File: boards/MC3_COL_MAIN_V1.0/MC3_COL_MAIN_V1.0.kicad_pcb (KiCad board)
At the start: 4 copper layers, 66 x 66 mm, 109 parts, among them J1 SUPPLY_IN, J10 MOTOR, J11 MOTOR, J12 CAN, J2 SWD, J3 ENC_leaf1, J4 ENC_leaf2, J5 ENC_leaf3, J6 ENC_leaf4, J7 MOTOR, J8 MOTOR, J9 MOTOR, Q1 AO4407C, SW1 SKRKAEE020, U1 AMS1117-3.3, U2 STM32F412RET6, U3 DRV8214RTER, U4 DRV8214RTER, U5 DRV8214RTER, U6 DRV8214RTER, U7 DRV8214RTER, U8 TJA1051T/3, Y1 8MHz

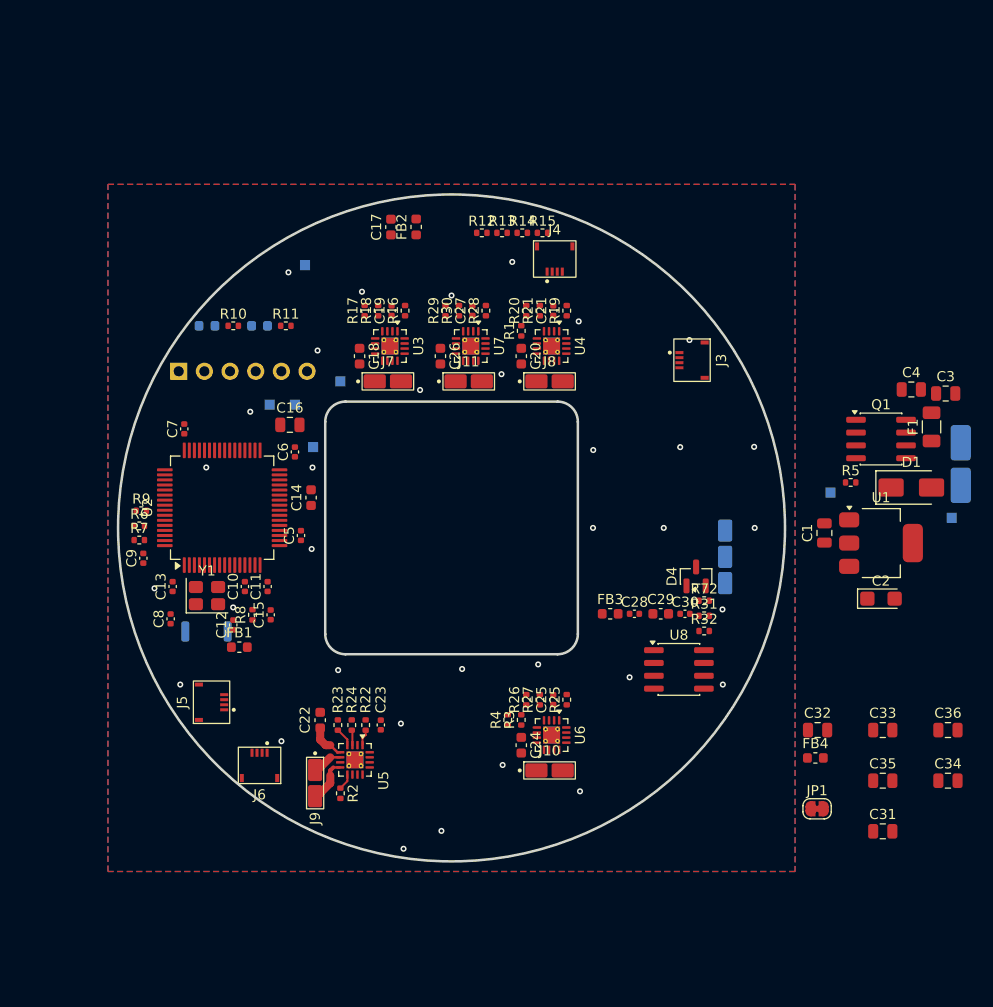
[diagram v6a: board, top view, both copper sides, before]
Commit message: PCB: power block placed on the east rim, input chain routed
Deleted the 19 GND stitching vias I had scattered across the board - they were
obstructing placement and one of them, at (75.726, 94.017), was sitting in the
middle of the MCU's 0.5 mm pin row and shorting RC_OUT_leaf3 to GND. My
collision check when generating them had a gap. They go back last, once the
layout settles. The 4 GND vias the user placed by hand are untouched.

Power block moved from its parking spot east of the outline into the free wedge
between the encoder FFC at 41 deg and the CAN block at 354 deg, which is where
the vault wants the supply pads - next to the CAN pads as one machine loom.
Layout was verified against pad overlap, rim and aperture before any part moved:
J1 (125, 89) on B.Cu, F1 (119.5, 88), Q1 (117, 92.5), D1 (124, 92) flipped so
its VIN_PROT pad faces the chain, R5 (113.9, 96.5), bulk C1/C3/C4 at y 96.5,
FB4 (116.5, 99), C32 (120, 99.5), U1 (118, 104), C2 (124, 100), TP1/TP2 on B.Cu.

Routed: VIN_PAD from J1 up through two 1.0/0.6 vias into F1, VIN_PROT through
Q1's four drain pads and out to D1 and TP2, Q1_G to R5, VM_LDO from the bead
through C32 to the regulator, +3V3 from the tab to C2. Widths 1.25-1.5 mm on the
input path, which carries the full 2 A - note VIN_PAD and VIN_PROT are still in
the Default netclass at 0.2 mm and should get a class of their own.

NOT routed, and left deliberately clean rather than shorted: VM distribution
from Q1 to the three bulk caps and the bead. The caps are oriented with their
GND pads across the VM bus path and Q1's gate pad blocks the southward escape,
so both attempts shorted. It needs the caps reoriented or the bus taken around
Q1 - flagged for review rather than guessed at again.

Co-Authored-By: Claude Opus 5 (1M context) <noreply@anthropic.com>
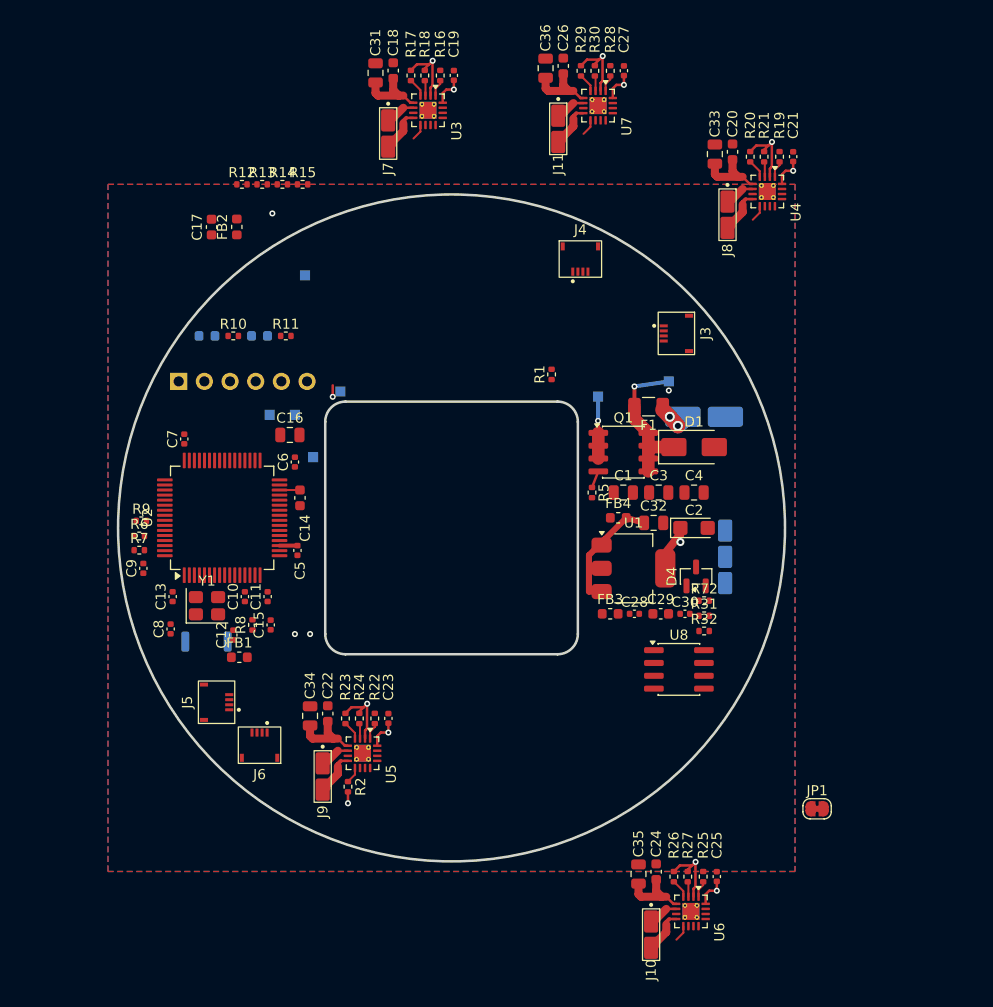
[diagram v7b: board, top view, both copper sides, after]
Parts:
- removed R3, R4: 2.2k, MC3_COL_MAIN:R_0402_1005Metric
- moved C31 90.3 mm to (92.5, 55.0), turned to 90 degrees
- moved C36 76.7 mm to (109.3, 54.5), turned to 90 degrees
- moved C34 63.5 mm to (86.0, 118.6), turned to 90 degrees
- moved C33 59.4 mm to (126.1, 63.0), turned to 90 degrees
- moved C26 31.2 mm to (111.1, 54.3), turned to 90 degrees
- moved TP2 31.1 mm to (121.5, 85.5)
- moved FB4 30.7 mm to (116.5, 99.0)
- moved C3 30.0 mm to (120.5, 96.5)
- moved C20 29.1 mm to (127.8, 62.8), turned to 90 degrees
- moved C18 28.5 mm to (94.2, 54.7), turned to 90 degrees
- moved C21 28.2 mm to (133.8, 63.3)
- moved C27 28.1 mm to (117.1, 54.8)
- moved F1 28.1 mm to (119.5, 88.0), turned to 180 degrees
- moved R30 27.3 mm to (114.2, 54.8), turned to -90 degrees
- moved R29 27.3 mm to (112.8, 54.8), turned to -90 degrees
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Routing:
- net +3V3: track 0.00 -> 56.0 mm, vias 0 -> 12
- net VM: track 3.65 -> 41.7 mm, vias 0 -> 1
- net VIN_PROT: track 0.00 -> 14.9 mm, vias 0 -> 2
- net /Power/VM_LDO: track 0.00 -> 11.9 mm
- net /leaf4/OUT2: track 0.00 -> 4.52 mm
- net /leaf1/OUT2: track 0.00 -> 4.52 mm
- net /leaf2/OUT2: track 0.00 -> 4.52 mm
- net /yaw/OUT2: track 0.00 -> 4.52 mm
- net /Power/VIN_PAD: track 0.00 -> 4.43 mm, vias 0 -> 2
- net GND: track 0.00 -> 4.39 mm, vias 34 -> 4
- net /leaf1/OUT1: track 0.00 -> 2.75 mm
- net /yaw/OUT1: track 0.00 -> 2.75 mm
- net /leaf4/OUT1: track 0.00 -> 2.75 mm
- net /leaf2/OUT1: track 0.00 -> 2.75 mm
- net /MCU/VCAP_1: track 0.00 -> 2.03 mm
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
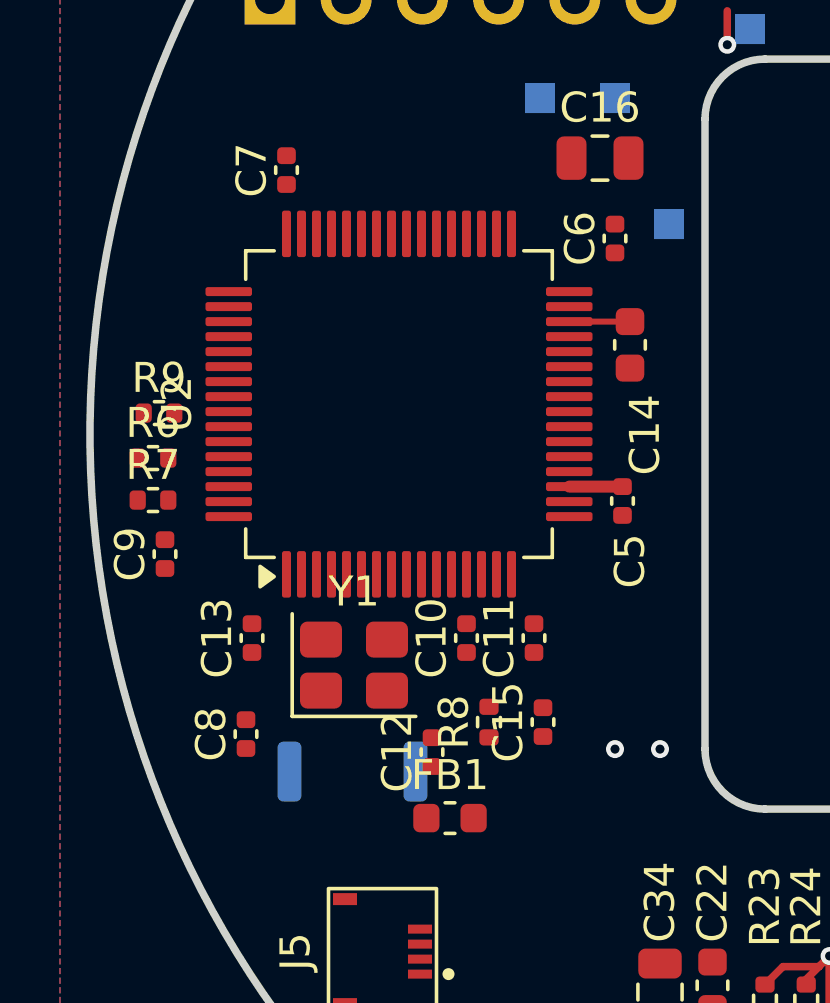
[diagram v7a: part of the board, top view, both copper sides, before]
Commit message: PCB: MCU local routing - decoupling, VDDA, crystal, BOOT0, I2C pull-ups
Placement needed no change: every VDD cap already sat 1.8-2.5 mm from its pin,
inside the vault's 3 mm budget, so this is routing only.

Routed, all on F.Cu with no via in any decoupling leg per the vault rule:
- VDD1 pin 19 -> C5 and VCAP_1 pin 30 -> C14 were already done
- VDD2 pin 32 -> C6, VDD3 pin 48 -> C7, VDD4 pin 64 -> C9, VBAT pin 1 -> C13
- VDDA pin 13 -> C10 -> C11, and FB1 down the corridor between C12 and R8
- crystal: pin 5 -> Y1.1 -> C8, pin 6 -> Y1.3 -> C12
- BOOT0 pin 60 -> R9, I2C pin 61 -> R6 and pin 62 -> R7

Two escapes had to be redone: pin 5 and pin 6 cannot leave diagonally, because
on a 0.5 mm pin row that crosses the neighbouring pads - OSC_IN shorted to pin 3
and OSC_OUT to pin 7 (NRST). Both now leave straight out of the pin row before
turning, and OSC_IN takes the west side of Y1 to avoid its GND pad.

GND pads are left to the F.Cu pour rather than routed.

The zones need refilling before DRC means anything - most remaining clearance
errors are trace-against-stale-fill, since the pour has not been recomputed
since these traces went in. Konnect has no refill tool, so that is a B in KiCad.

Co-Authored-By: Claude Opus 5 (1M context) <noreply@anthropic.com>
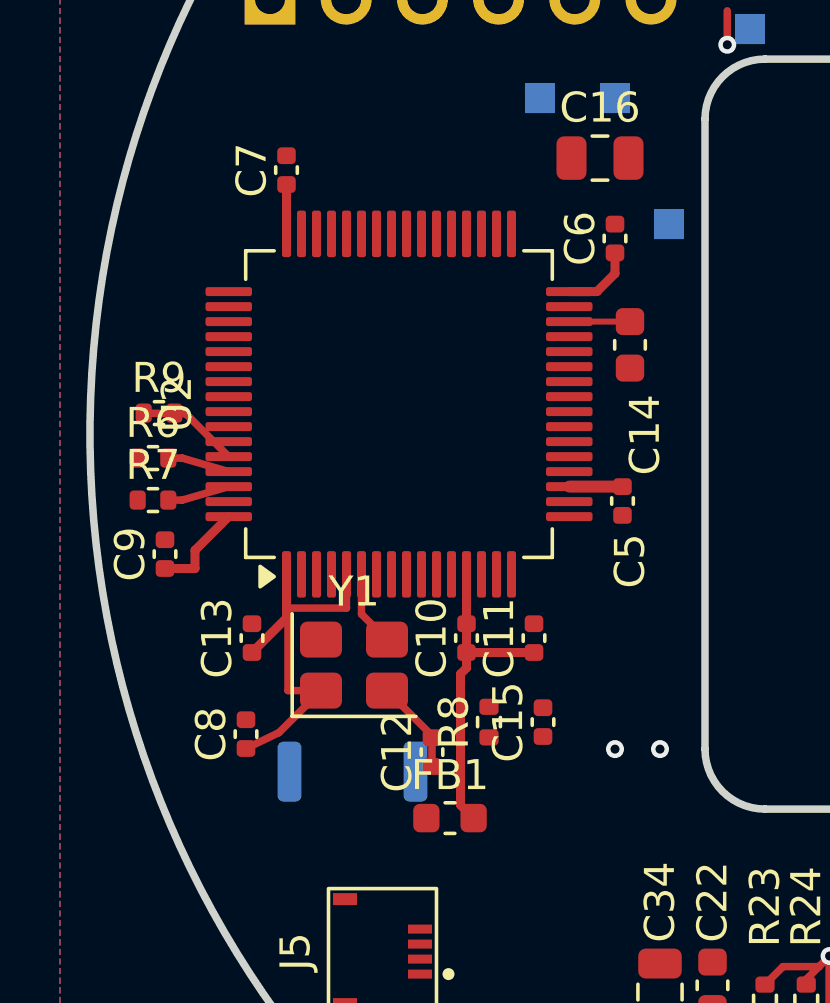
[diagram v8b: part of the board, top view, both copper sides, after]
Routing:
- net /MCU/VDDA: track 0.00 -> 10.6 mm
- net +3V3: track 56.0 -> 66.4 mm
- net /MCU/OSC_IN: track 0.00 -> 10.1 mm
- net /MCU/OSC_OUT: track 0.00 -> 3.56 mm
- net /MCU/BOOT0: track 0.00 -> 3.43 mm
- net GND: track 4.39 -> 6.51 mm
- net I2C1_SDA: track 0.00 -> 2.08 mm
- net I2C1_SCL: track 0.00 -> 2.08 mm
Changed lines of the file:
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@@
+		(net "GND")
+	)
+	(segment
+		(start 76.9 108.55)
+		(end 78.4 110.05)
+		(width 0.25)
+		(layer "F.Cu")
 		(net "GND")
 	)
@@
 	)
 	(segment
+		(start 82.975 95.25)
+		(end 83.9 95.25)
+		(width 0.3)
+		(layer "F.Cu")
+		(net "+3V3")
+	)
+	(segment
 		(start 93.75 120.25)
 		(end 93 120.25)
@@
 	)
 	(segment
+		(start 84.5 94.65)
+		(end 84.5 93.96)
+		(width 0.3)
+		(layer "F.Cu")
+		(net "+3V3")
+	)
+	(segment
+		(start 71.625 102.75)
+		(end 70.5 103.875)
+		(width 0.3)
+		(layer "F.Cu")
+		(net "+3V3")
+	)
+	(segment
 		(start 133.058501 64.657386)
 		(end 132.7075 65.008387)
@@
 	)
 	(segment
+		(start 70.5 104.48)
+		(end 69.5 104.48)
+		(width 0.3)
+		(layer "F.Cu")
+		(net "+3V3")
+	)
+	(segment
 		(start 131.5 64.465887)
 		(end 131.5 65.25)
@@
 	)
 	(segment
+		(start 70.5 103.875)
+		(end 70.5 104.48)
+		(width 0.3)
+		(layer "F.Cu")
+		(net "+3V3")
+	)
+	(segment
 		(start 100.228501 56.619886)
 		(end 100.228501 55.698772)
@@
 	)
 	(segment
+		(start 73.55 106.13)
+		(end 72.4 107.28)
+		(width 0.3)
+		(layer "F.Cu")
+		(net "+3V3")
+	)
+	(segment
 		(start 96.577387 54.119886)
 		(end 95.978501 54.718772)
@@
 	)
 	(segment
+		(start 73.55 93.325)
+		(end 73.55 91.68)
+		(width 0.3)
+		(layer "F.Cu")
+		(net "+3V3")
+	)
+	(segment
 		(start 90.875001 118.175036)
 		(end 90.875001 118.348886)
@@
 		(end 122.65 100.6)
 		(width 0.8)
+		(layer "F.Cu")
+		(net "+3V3")
+	)
+	(segment
+		(start 83.9 95.25)
+		(end 84.5 94.65)
+		(width 0.3)
 		(layer "F.Cu")
 		(net "+3V3")
@@
 		(end 125.148999 136.252115)
 		(width 0.25)
+		(layer "F.Cu")
+		(net "+3V3")
+	)
+	(segment
+		(start 73.55 104.675)
+		(end 73.55 106.13)
+		(width 0.3)
 		(layer "F.Cu")
 		(net "+3V3")
@@
 	)
 	(segment
+		(start 70.075 102.2)
+		(end 69.61 102.2)
+		(width 0.25)
+		(layer "F.Cu")
+		(net "I2C1_SDA")
+	)
+	(segment
+		(start 71.625 101.75)
+		(end 70.075 102.2)
+		(width 0.25)
+		(layer "F.Cu")
+		(net "I2C1_SDA")
+	)
+	(segment
 		(start 122.941499 135.941499)
 		(end 122.941499 136.493727)
@@
 	)
 	(segment
+		(start 71.625 101.25)
+		(end 70.075 100.8)
+		(width 0.25)
+		(layer "F.Cu")
+		(net "I2C1_SCL")
+	)
+	(segment
+		(start 70.075 100.8)
+		(end 69.61 100.8)
+		(width 0.25)
+		(layer "F.Cu")
+		(net "I2C1_SCL")
+	)
+	(segment
+		(start 73.6 105.8)
+		(end 73.6 108.55)
+		(width 0.25)
+		(layer "F.Cu")
+		(net "/MCU/OSC_IN")
+	)
+	(segment
+		(start 75.55 104.675)
+		(end 75.55 105.8)
+		(width 0.25)
+		(layer "F.Cu")
+		(net "/MCU/OSC_IN")
+	)
+	(segment
+		(start 73.3 109.95)
+		(end 72.2 110.48)
+		(width 0.25)
+		(layer "F.Cu")
+		(net "/MCU/OSC_IN")
+	)
+	(segment
+		(start 73.6 108.55)
+		(end 74.7 108.55)
+		(width 0.25)
+		(layer "F.Cu")
+		(net "/MCU/OSC_IN")
+	)
+	(segment
+		(start 75.55 105.8)
+		(end 73.6 105.8)
+		(width 0.25)
+		(layer "F.Cu")
+		(net "/MCU/OSC_IN")
+	)
+	(segment
+		(start 74.7 108.55)
+		(end 73.3 109.95)
+		(width 0.25)
+		(layer "F.Cu")
+		(net "/MCU/OSC_IN")
+	)
+	(segment
+		(start 76.05 106)
+		(end 76.9 106.85)
+		(width 0.25)
+		(layer "F.Cu")
+		(net "/MCU/OSC_OUT")
+	)
+	(segment
+		(start 78.4 110.05)
+		(end 78.4 111.08)
+		(width 0.25)
+		(layer "F.Cu")
+		(net "/MCU/OSC_OUT")
+	)
+	(segment
+		(start 76.05 104.675)
+		(end 76.05 106)
+		(width 0.25)
+		(layer "F.Cu")
+		(net "/MCU/OSC_OUT")
+	)
+	(segment
 		(start 117.29 99)
 		(end 119.05 99.5)
@@
 	)
 	(segment
+		(start 79.35 112.363)
+		(end 79.35 107.995)
+		(width 0.3)
+		(layer "F.Cu")
+		(net "/MCU/VDDA")
+	)
+	(segment
+		(start 79.787 112.8)
+		(end 79.35 112.363)
+		(width 0.3)
+		(layer "F.Cu")
+		(net "/MCU/VDDA")
+	)
+	(segment
+		(start 79.55 107.28)
+		(end 81.8 107.28)
+		(width 0.3)
+		(layer "F.Cu")
+		(net "/MCU/VDDA")
+	)
+	(segment
+		(start 79.55 104.675)
+		(end 79.55 107.28)
+		(width 0.3)
+		(layer "F.Cu")
+		(net "/MCU/VDDA")
+	)
+	(segment
+		(start 79.35 107.995)
+		(end 79.55 107.795)
+		(width 0.3)
+		(layer "F.Cu")
+		(net "/MCU/VDDA")
+	)
+	(segment
+		(start 79.55 107.795)
+		(end 79.55 107.28)
+		(width 0.3)
+		(layer "F.Cu")
+		(net "/MCU/VDDA")
+	)
+	(segment
 		(start 82.975 96.25)
 		(end 85 96.25)
@@
 	)
 	(segment
+		(start 71.625 100.75)
+		(end 70.2 99.325)
+		(width 0.25)
+		(layer "F.Cu")
+		(net "/MCU/BOOT0")
+	)
+	(segment
+		(start 70.2 99.325)
+		(end 68.79 99.3)
+		(width 0.25)
+		(layer "F.Cu")
+		(net "/MCU/BOOT0")
+	)
+	(segment
